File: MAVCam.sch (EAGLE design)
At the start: 15 parts, among them IC1 PIC24FJ64GA002_QFN, J201 DF13C-6P-1.25V, U4 TS3USB30EDGSR

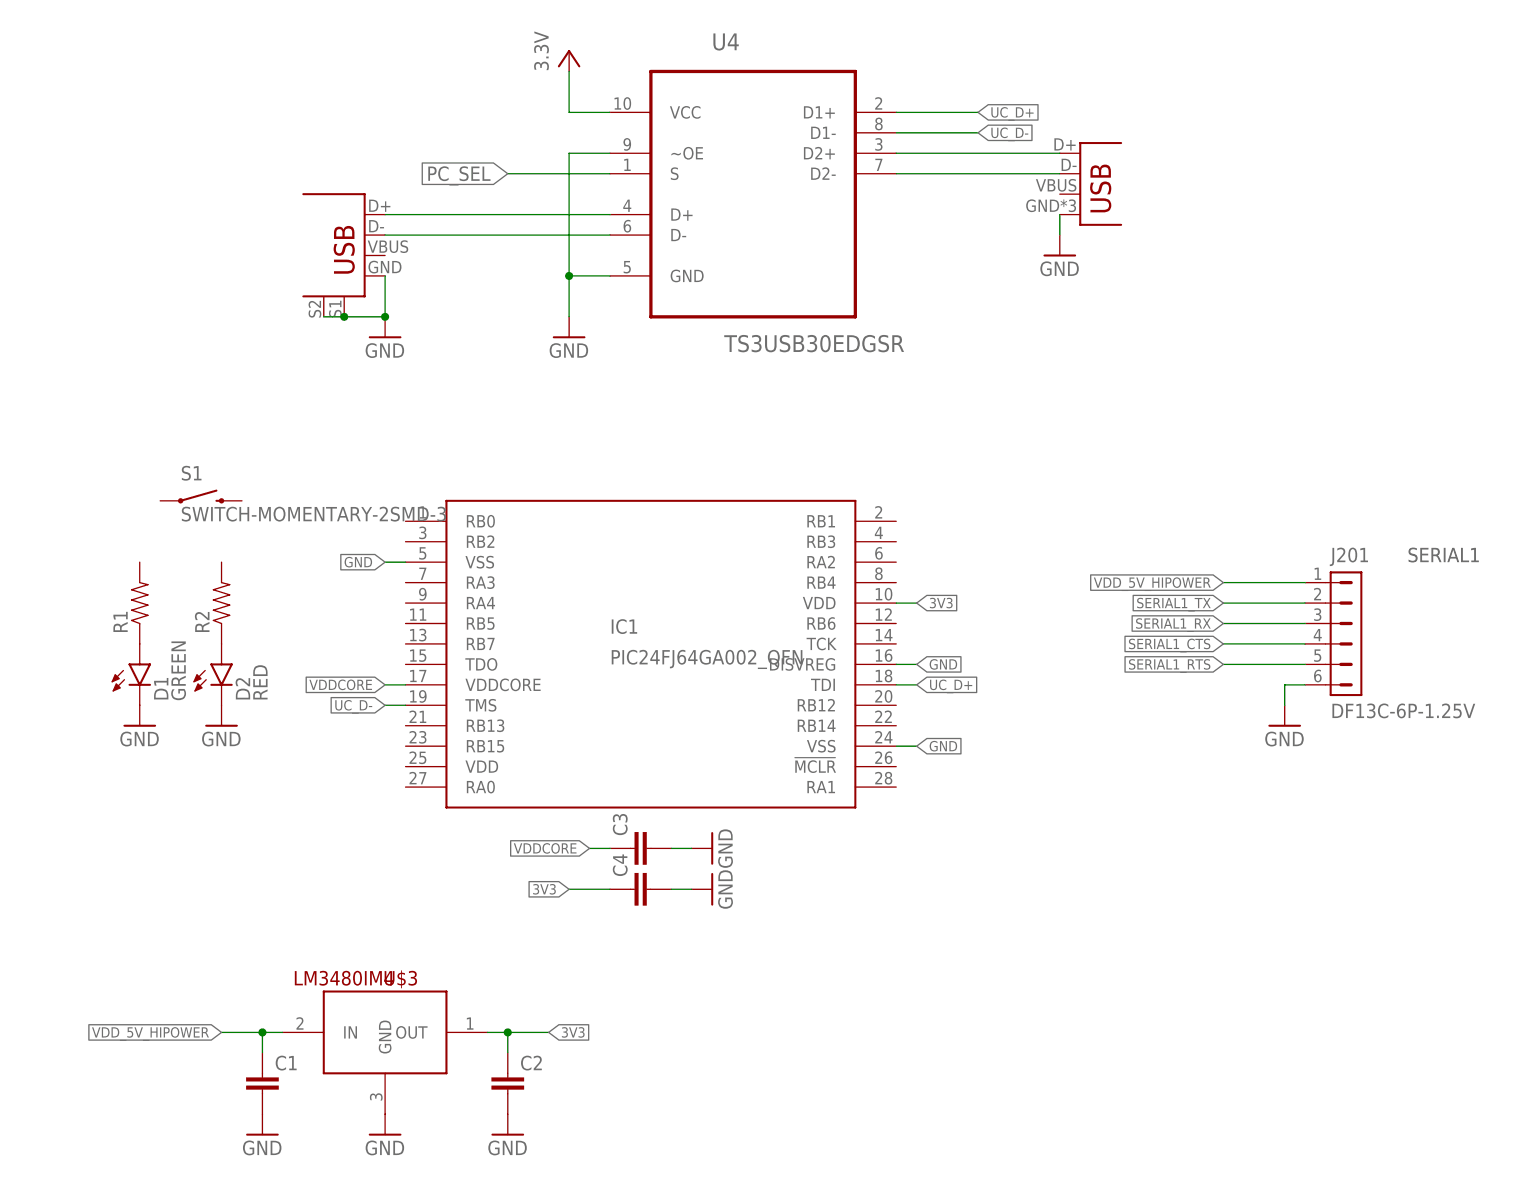
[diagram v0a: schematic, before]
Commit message: Finishing routing
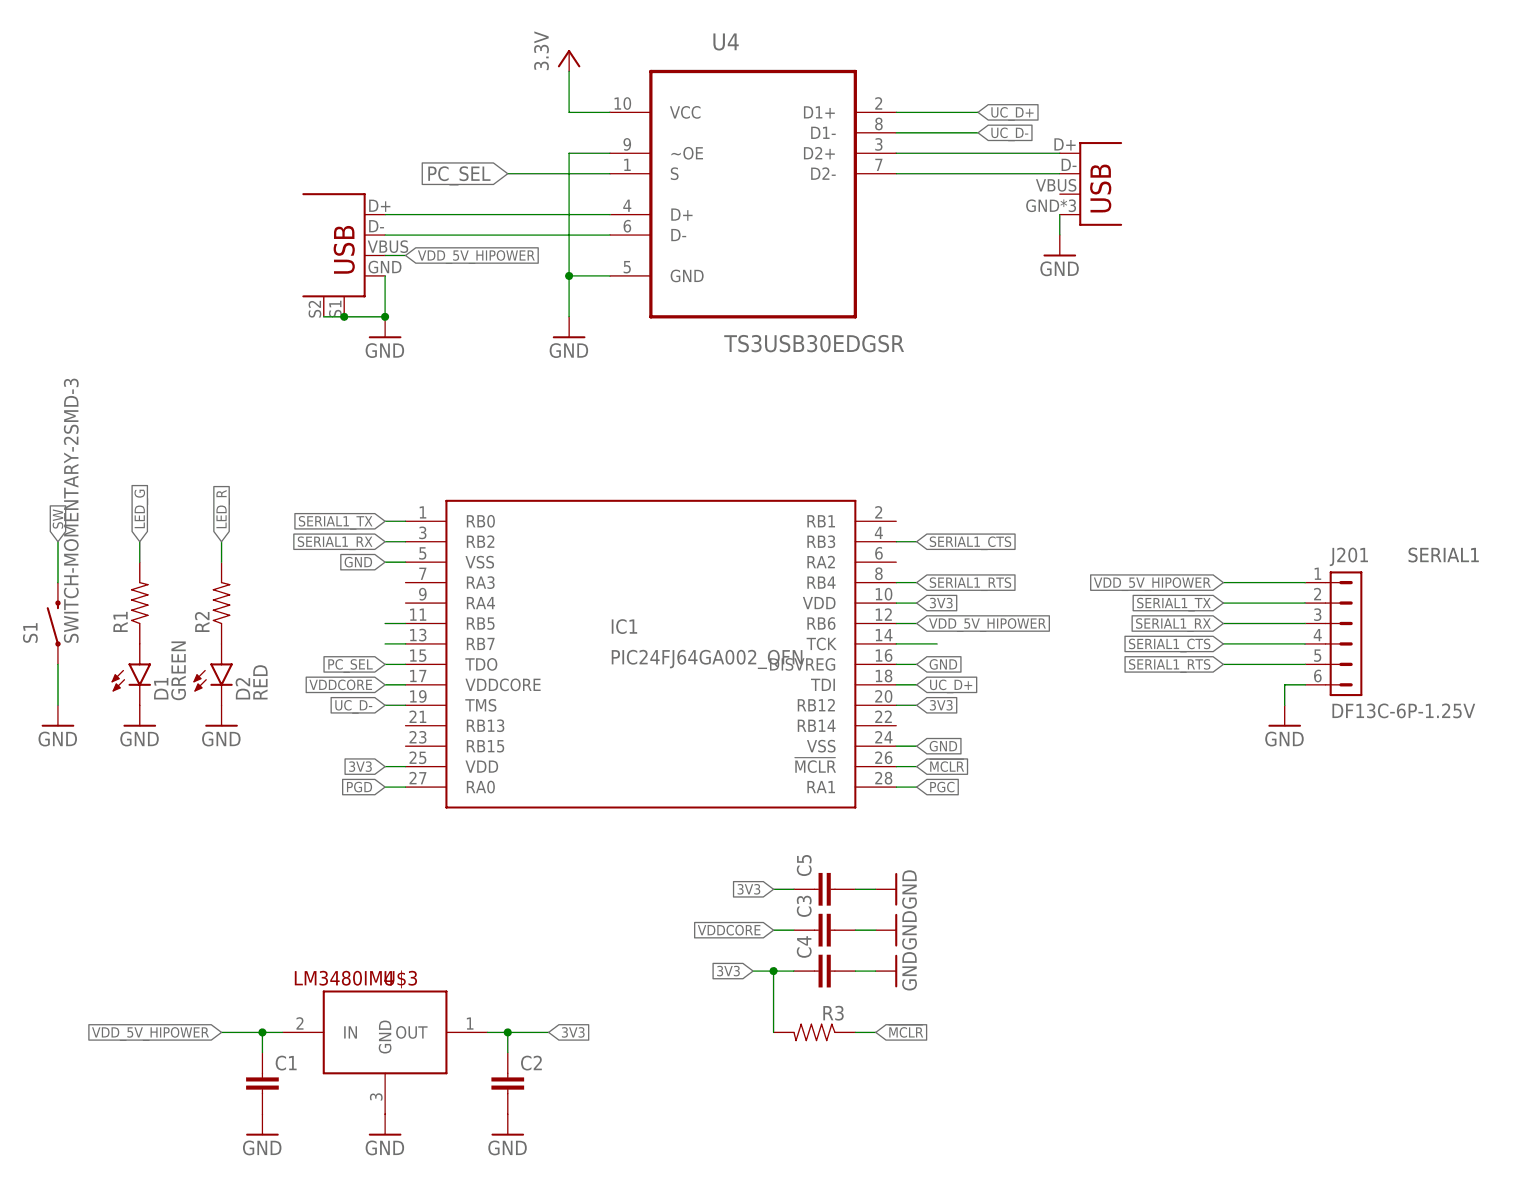
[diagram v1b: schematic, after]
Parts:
- added C5: (no value), SparkFun-Passives:CAP0603-CAP
- added R3: (no value), SparkFun-Passives:RESISTOR0603-RES
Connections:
- new net !MCLR: IC1.!MCLR, R3.1
- new net LED_G: IC1.RB7, R1.2
- new net LED_R: IC1.RB5, R2.2
- new net PGC: IC1.RA1
- new net PGD: IC1.RA0
- new net SW: IC1.TCK, S1.2
- net 3V3: now also C5.1, IC1.RB12, IC1.VDD@2, R3.2
- net GND: now also C5.2, S1.1
- net PC_SEL: now also IC1.TDO
- net SERIAL1_CTS: now also IC1.RB3
- net SERIAL1_RTS: now also IC1.RB4
- net SERIAL1_RX: now also IC1.RB2
- net SERIAL1_TX: now also IC1.RB0
- net VDD_5V_HIPOWER: now also IC1.RB6, U$1.VBUS
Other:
- moved on the sheet: C3, C4, S1
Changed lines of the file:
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@@
 <part name="C4" library="SparkFun-Passives" deviceset="CAP" device="0603-CAP"/>
 <part name="GND10" library="pixhawk2" deviceset="GND" device=""/>
+<part name="R3" library="SparkFun-Passives" deviceset="RESISTOR" device="0603-RES"/>
+<part name="GND11" library="pixhawk2" deviceset="GND" device=""/>
+<part name="C5" library="SparkFun-Passives" deviceset="CAP" device="0603-CAP"/>
+<part name="GND12" library="pixhawk2" deviceset="GND" device=""/>
 </parts>
 <sheets>
@@
 <instance part="D1" gate="G$1" x="-10.16" y="88.9"/>
 <instance part="D2" gate="G$1" x="0" y="88.9"/>
-<instance part="S1" gate="G$1" x="-2.54" y="109.22"/>
+<instance part="S1" gate="G$1" x="-20.32" y="93.98" rot="R90"/>
 <instance part="U$3" gate="G$1" x="20.32" y="43.18"/>
 <instance part="C1" gate="G$1" x="5.08" y="35.56"/>
@@
 <instance part="GND3" gate="1" x="5.08" y="30.48"/>
 <instance part="GND4" gate="1" x="20.32" y="129.54"/>
-<instance part="C3" gate="G$1" x="53.34" y="66.04" rot="R90"/>
-<instance part="GND6" gate="1" x="60.96" y="66.04" rot="R90"/>
+<instance part="C3" gate="G$1" x="76.2" y="55.88" rot="R90"/>
+<instance part="GND6" gate="1" x="83.82" y="55.88" rot="R90"/>
 <instance part="GND7" gate="1" x="104.14" y="139.7"/>
 <instance part="R1" gate="G$1" x="-10.16" y="96.52" rot="R90"/>
@@
 <instance part="GND8" gate="1" x="-10.16" y="81.28"/>
 <instance part="GND9" gate="1" x="0" y="81.28"/>
-<instance part="C4" gate="G$1" x="53.34" y="60.96" rot="R90"/>
-<instance part="GND10" gate="1" x="60.96" y="60.96" rot="R90"/>
+<instance part="C4" gate="G$1" x="76.2" y="50.8" rot="R90"/>
+<instance part="GND10" gate="1" x="83.82" y="50.8" rot="R90"/>
+<instance part="R3" gate="G$1" x="73.66" y="43.18" rot="MR0"/>
+<instance part="GND11" gate="1" x="-20.32" y="81.28"/>
+<instance part="C5" gate="G$1" x="76.2" y="60.96" rot="R90"/>
+<instance part="GND12" gate="1" x="83.82" y="60.96" rot="R90"/>
 </instances>
 <busses>
@@
 <pinref part="C3" gate="G$1" pin="2"/>
 <pinref part="GND6" gate="1" pin="GND"/>
-<wire x1="58.42" y1="66.04" x2="55.88" y2="66.04" width="0.1524" layer="91"/>
+<wire x1="81.28" y1="55.88" x2="78.74" y2="55.88" width="0.1524" layer="91"/>
 </segment>
 <segment>
@@
 <pinref part="C4" gate="G$1" pin="2"/>
 <pinref part="GND10" gate="1" pin="GND"/>
-<wire x1="58.42" y1="60.96" x2="55.88" y2="60.96" width="0.1524" layer="91"/>
+<wire x1="81.28" y1="50.8" x2="78.74" y2="50.8" width="0.1524" layer="91"/>
+</segment>
+<segment>
+<pinref part="S1" gate="G$1" pin="1"/>
+<pinref part="GND11" gate="1" pin="GND"/>
+<wire x1="-20.32" y1="83.82" x2="-20.32" y2="88.9" width="0.1524" layer="91"/>
+</segment>
+<segment>
+<pinref part="C5" gate="G$1" pin="2"/>
+<pinref part="GND12" gate="1" pin="GND"/>
+<wire x1="78.74" y1="60.96" x2="81.28" y2="60.96" width="0.1524" layer="91"/>
 </segment>
 </net>
@@
 <pinref part="J201" gate="G$1" pin="4"/>
 </segment>
+<segment>
+<wire x1="86.36" y1="104.14" x2="83.82" y2="104.14" width="0.1524" layer="91"/>
+<pinref part="IC1" gate="G$1" pin="RB3"/>
+<label x="86.36" y="104.14" size="1.27" layer="95" xref="yes"/>
+</segment>
 </net>
 <net name="SERIAL1_RTS" class="0">
@@
 <pinref part="J201" gate="G$1" pin="5"/>
 </segment>
+<segment>
+<wire x1="86.36" y1="99.06" x2="83.82" y2="99.06" width="0.1524" layer="91"/>
+<pinref part="IC1" gate="G$1" pin="RB4"/>
+<label x="86.36" y="99.06" size="1.27" layer="95" xref="yes"/>
+</segment>
 </net>
 <net name="SERIAL1_TX" class="0">
@@
 <pinref part="J201" gate="G$1" pin="2"/>
 </segment>
+<segment>
+<wire x1="22.86" y1="106.68" x2="20.32" y2="106.68" width="0.1524" layer="91"/>
+<pinref part="IC1" gate="G$1" pin="RB0"/>
+<label x="20.32" y="106.68" size="1.27" layer="95" rot="R180" xref="yes"/>
+</segment>
 </net>
 <net name="SERIAL1_RX" class="0">
@@
 <label x="124.46" y="93.98" size="1.27" layer="95" rot="R180" xref="yes"/>
 <pinref part="J201" gate="G$1" pin="3"/>
+</segment>
+<segment>
+<wire x1="22.86" y1="104.14" x2="20.32" y2="104.14" width="0.1524" layer="91"/>
+<pinref part="IC1" gate="G$1" pin="RB2"/>
+<label x="20.32" y="104.14" size="1.27" layer="95" rot="R180" xref="yes"/>
 </segment>
 </net>
@@
 <label x="0" y="43.18" size="1.27" layer="95" rot="R180" xref="yes"/>
 </segment>
+<segment>
+<pinref part="IC1" gate="G$1" pin="RB6"/>
+<wire x1="83.82" y1="93.98" x2="86.36" y2="93.98" width="0.1524" layer="91"/>
+<label x="86.36" y="93.98" size="1.27" layer="95" xref="yes"/>
+</segment>
+<segment>
+<pinref part="U$1" gate="G$1" pin="VBUS"/>
+<wire x1="20.32" y1="139.7" x2="22.86" y2="139.7" width="0.1524" layer="91"/>
+<label x="22.86" y="139.7" size="1.27" layer="95" xref="yes"/>
+</segment>
 </net>
 <net name="PC_D-" class="0">
@@
 <wire x1="48.26" y1="149.86" x2="35.56" y2="149.86" width="0.1524" layer="91"/>
 <label x="35.56" y="149.86" size="1.778" layer="95" rot="R180" xref="yes"/>
+</segment>
+<segment>
+<wire x1="22.86" y1="88.9" x2="20.32" y2="88.9" width="0.1524" layer="91"/>
+<label x="20.32" y="88.9" size="1.27" layer="95" rot="R180" xref="yes"/>
+<pinref part="IC1" gate="G$1" pin="TDO"/>
 </segment>
 </net>
@@
 </segment>
 <segment>
-<wire x1="43.18" y1="60.96" x2="48.26" y2="60.96" width="0.1524" layer="91"/>
+<wire x1="66.04" y1="50.8" x2="68.58" y2="50.8" width="0.1524" layer="91"/>
 <pinref part="C4" gate="G$1" pin="1"/>
-<label x="43.18" y="60.96" size="1.27" layer="95" rot="R180" xref="yes"/>
+<label x="66.04" y="50.8" size="1.27" layer="95" rot="R180" xref="yes"/>
+<pinref part="R3" gate="G$1" pin="2"/>
+<wire x1="68.58" y1="50.8" x2="71.12" y2="50.8" width="0.1524" layer="91"/>
+<wire x1="68.58" y1="43.18" x2="68.58" y2="50.8" width="0.1524" layer="91"/>
+<junction x="68.58" y="50.8"/>
+</segment>
+<segment>
+<wire x1="20.32" y1="76.2" x2="22.86" y2="76.2" width="0.1524" layer="91"/>
+<pinref part="IC1" gate="G$1" pin="VDD@2"/>
+<label x="20.32" y="76.2" size="1.27" layer="95" rot="R180" xref="yes"/>
+</segment>
+<segment>
+<pinref part="C5" gate="G$1" pin="1"/>
+<wire x1="71.12" y1="60.96" x2="68.58" y2="60.96" width="0.1524" layer="91"/>
+<label x="68.58" y="60.96" size="1.27" layer="95" rot="R180" xref="yes"/>
+</segment>
+<segment>
+<pinref part="IC1" gate="G$1" pin="RB12"/>
+<wire x1="83.82" y1="83.82" x2="86.36" y2="83.82" width="0.1524" layer="91"/>
+<label x="86.36" y="83.82" size="1.27" layer="95" xref="yes"/>
 </segment>
 </net>
@@
 </segment>
 <segment>
-<wire x1="45.72" y1="66.04" x2="48.26" y2="66.04" width="0.1524" layer="91"/>
+<wire x1="68.58" y1="55.88" x2="71.12" y2="55.88" width="0.1524" layer="91"/>
 <pinref part="C3" gate="G$1" pin="1"/>
-<label x="45.72" y="66.04" size="1.27" layer="95" rot="R180" xref="yes"/>
+<label x="68.58" y="55.88" size="1.27" layer="95" rot="R180" xref="yes"/>
 </segment>
 </net>
@@
 </segment>
 </net>
+<net name="!MCLR" class="0">
+<segment>
+<pinref part="IC1" gate="G$1" pin="!MCLR"/>
+<wire x1="83.82" y1="76.2" x2="86.36" y2="76.2" width="0.1524" layer="91"/>
+<label x="86.36" y="76.2" size="1.27" layer="95" xref="yes"/>
+</segment>
+<segment>
+<pinref part="R3" gate="G$1" pin="1"/>
+<wire x1="78.74" y1="43.18" x2="81.28" y2="43.18" width="0.1524" layer="91"/>
+<label x="81.28" y="43.18" size="1.27" layer="95" xref="yes"/>
+</segment>
+</net>
+<net name="PGC" class="0">
+<segment>
+<pinref part="IC1" gate="G$1" pin="RA1"/>
+<wire x1="83.82" y1="73.66" x2="86.36" y2="73.66" width="0.1524" layer="91"/>
+<label x="86.36" y="73.66" size="1.27" layer="95" xref="yes"/>
+</segment>
+</net>
+<net name="PGD" class="0">
+<segment>
+<pinref part="IC1" gate="G$1" pin="RA0"/>
+<wire x1="20.32" y1="73.66" x2="22.86" y2="73.66" width="0.1524" layer="91"/>
+<label x="20.32" y="73.66" size="1.27" layer="95" rot="R180" xref="yes"/>
+</segment>
+</net>
+<net name="SW" class="0">
+<segment>
+<pinref part="S1" gate="G$1" pin="2"/>
+<wire x1="-20.32" y1="99.06" x2="-20.32" y2="104.14" width="0.1524" layer="91"/>
+<label x="-20.32" y="104.14" size="1.27" layer="95" rot="R90" xref="yes"/>
+</segment>
+<segment>
+<wire x1="88.9" y1="91.44" x2="83.82" y2="91.44" width="0.1524" layer="91"/>
+<pinref part="IC1" gate="G$1" pin="TCK"/>
+</segment>
+</net>
+<net name="LED_G" class="0">
+<segment>
+<pinref part="R1" gate="G$1" pin="2"/>
+<wire x1="-10.16" y1="101.6" x2="-10.16" y2="104.14" width="0.1524" layer="91"/>
+<label x="-10.16" y="104.14" size="1.27" layer="95" rot="R90" xref="yes"/>
+</segment>
+<segment>
+<wire x1="22.86" y1="91.44" x2="20.32" y2="91.44" width="0.1524" layer="91"/>
+<pinref part="IC1" gate="G$1" pin="RB7"/>
+</segment>
+</net>
+<net name="LED_R" class="0">
+<segment>
+<pinref part="R2" gate="G$1" pin="2"/>
+<wire x1="0" y1="101.6" x2="0" y2="104.14" width="0.1524" layer="91"/>
+<label x="0" y="104.14" size="1.27" layer="95" rot="R90" xref="yes"/>
+</segment>
+<segment>
+<wire x1="22.86" y1="93.98" x2="20.32" y2="93.98" width="0.1524" layer="91"/>
+<pinref part="IC1" gate="G$1" pin="RB5"/>
+</segment>
+</net>
